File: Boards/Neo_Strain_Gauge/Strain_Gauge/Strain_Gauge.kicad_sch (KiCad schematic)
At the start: 70 parts, among them J1 Screw_Terminal_01x03, J2 Screw_Terminal_01x03, J3 Screw_Terminal_01x03, J4 Screw_Terminal_01x03, J5 Conn_01x02, J6 USB_B_Micro, J7 Conn_02x10_Counter_Clockwise, J8 Conn_02x12_Counter_Clockwise, U1 W25Q128JVS, U2 NCP1117-3.3_SOT223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

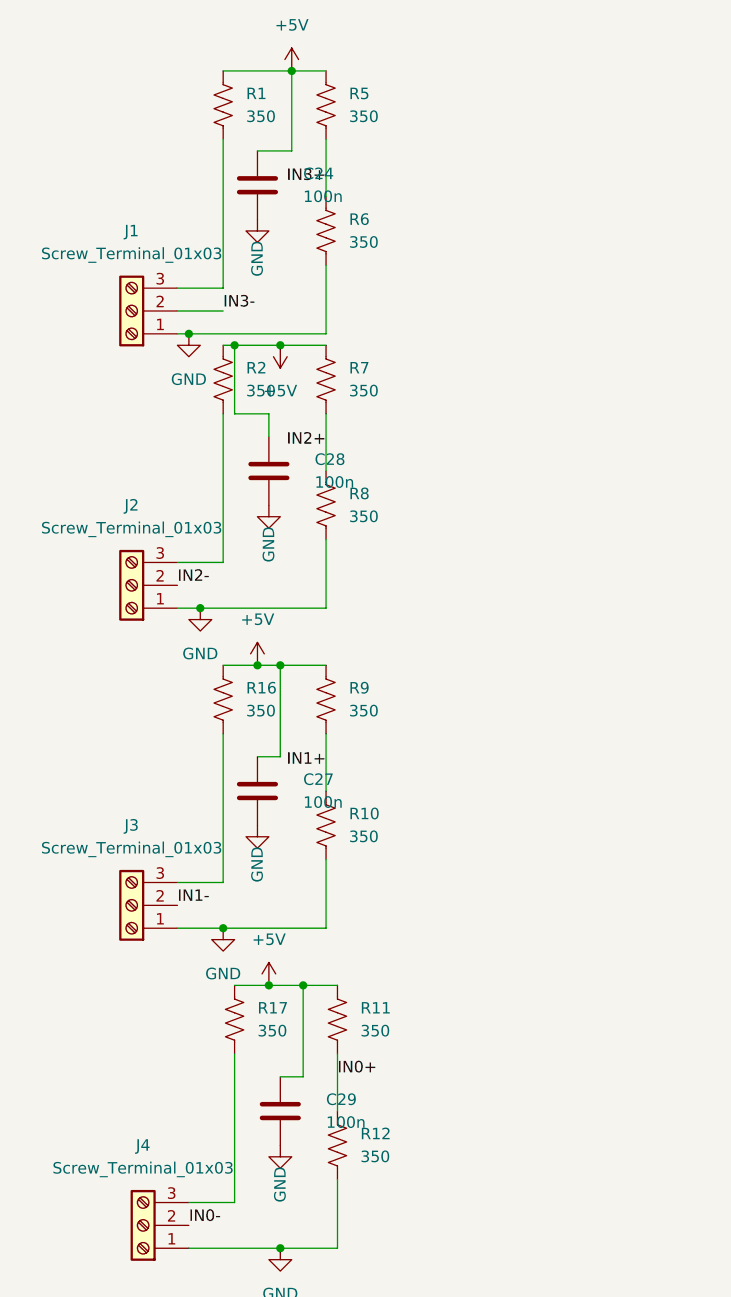
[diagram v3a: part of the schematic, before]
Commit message: Better BOM and more accurate to final design schematic, little will change from this.
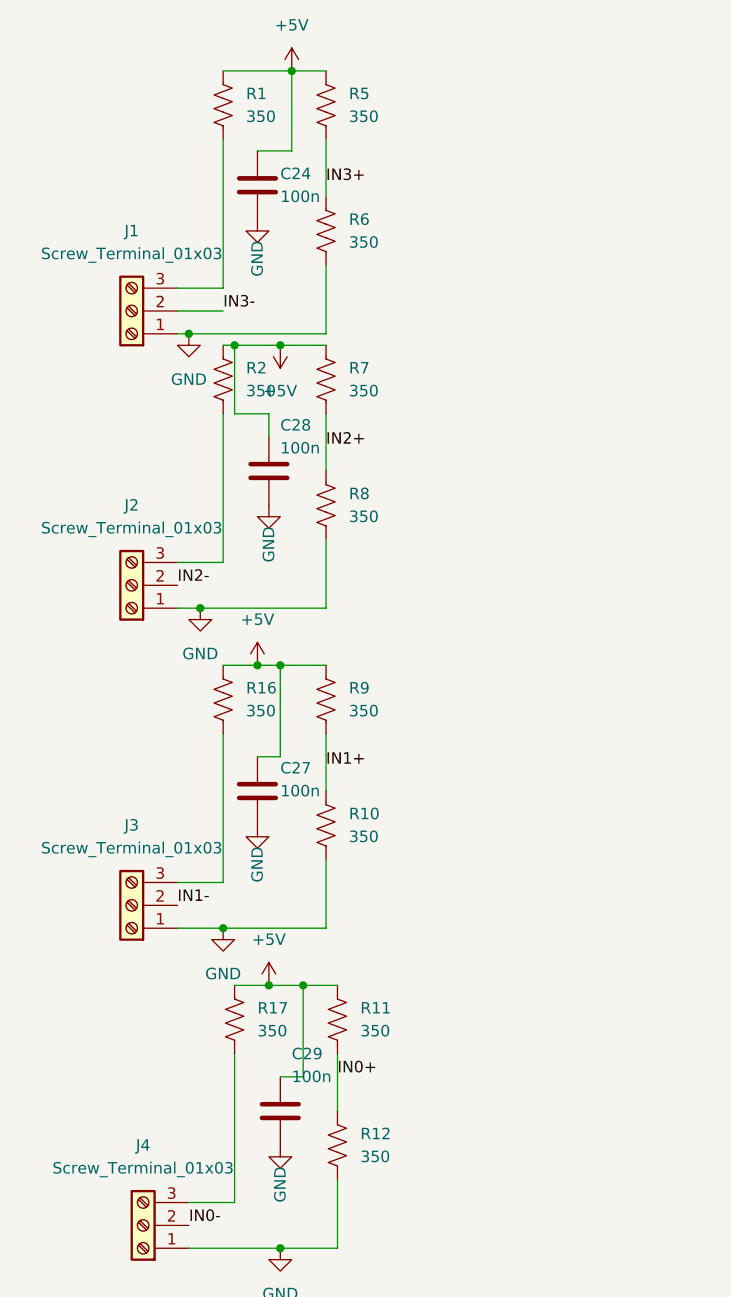
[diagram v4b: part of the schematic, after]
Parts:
- J1, J2, J3, J4: footprint TerminalBlock:TerminalBlock_Altech_AK300-3_P5.00mm -> TerminalBlock_Phoenix:TerminalBlock_Phoenix_PT-1,5-3-3.5-H_1x03_P3.50mm_Horizontal; Purchase Link (none) -> https://www.digikey.com/en/products/detail/phoenix-contact/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
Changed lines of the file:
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@@
     (effects (font (size 1.27 1.27)) (justify right bottom))
   )
-  (label "IN1+" (at -217.17 331.47 180)
-    (effects (font (size 1.27 1.27)) (justify right bottom))
+  (label "IN1+" (at -217.17 331.47 0)
+    (effects (font (size 1.27 1.27)) (justify left bottom))
   )
   (label "GPIO28_ADC2" (at 238.76 417.83 180)
@@
     (effects (font (size 1.27 1.27)) (justify right bottom))
   )
-  (label "IN3+" (at -217.17 266.609 180)
-    (effects (font (size 1.27 1.27)) (justify right bottom))
+  (label "IN3+" (at -217.17 266.609 0)
+    (effects (font (size 1.27 1.27)) (justify left bottom))
   )
   (label "USB_D+" (at 242.57 267.97 180)
@@
     (effects (font (size 1.27 1.27)) (justify right bottom))
   )
-  (label "IN2+" (at -217.17 295.91 180)
-    (effects (font (size 1.27 1.27)) (justify right bottom))
+  (label "IN2+" (at -217.17 295.91 0)
+    (effects (font (size 1.27 1.27)) (justify left bottom))
   )
   (label "GPIO7" (at 406.4 332.74 180)
@@
   )
   (symbol (lib_id "Device:C") (at -223.52 298.45 180) (unit 1)
-    (in_bom yes) (on_board yes) (fields_autoplaced)
-    (property "Reference" "C28" (id 0) (at -218.44 297.1799 0)
+    (in_bom yes) (on_board yes)
+    (property "Reference" "C28" (id 0) (at -222.25 293.37 0)
       (effects (font (size 1.27 1.27)) (justify right))
     )
-    (property "Value" "100n" (id 1) (at -218.44 299.7199 0)
+    (property "Value" "100n" (id 1) (at -222.25 295.91 0)
       (effects (font (size 1.27 1.27)) (justify right))
     )
@@
   )
   (symbol (lib_id "Device:C") (at -224.79 266.7 180) (unit 1)
-    (in_bom yes) (on_board yes) (fields_autoplaced)
-    (property "Reference" "C24" (id 0) (at -219.71 265.4299 0)
+    (in_bom yes) (on_board yes)
+    (property "Reference" "C24" (id 0) (at -222.25 265.43 0)
       (effects (font (size 1.27 1.27)) (justify right))
     )
-    (property "Value" "100n" (id 1) (at -219.71 267.9699 0)
+    (property "Value" "100n" (id 1) (at -222.25 267.97 0)
       (effects (font (size 1.27 1.27)) (justify right))
     )
@@
     (property "Reference" "J3" (id 0) (at -238.76 337.82 0))
     (property "Value" "Screw_Terminal_01x03" (id 1) (at -238.76 340.36 0))
-    (property "Footprint" "TerminalBlock:TerminalBlock_Altech_AK300-3_P5.00mm" (id 2) (at -238.76 346.71 0)
+    (property "Footprint" "TerminalBlock_Phoenix:TerminalBlock_Phoenix_PT-1,5-3-3.5-H_1x03_P3.50mm_Horizontal" (id 2) (at -238.76 346.71 0)
       (effects (font (size 1.27 1.27)) hide)
     )
@@
       (effects (font (size 1.27 1.27)) hide)
     )
+    (property "Purchase Link" "https://www.digikey.com/en/products/detail/phoenix-contact/1751251/2511152" (id 4) (at -238.76 346.71 0)
+      (effects (font (size 1.27 1.27)) hide)
+    )
     (pin "1")
     (pin "2")
@@
     (property "Reference" "J1" (id 0) (at -238.76 271.78 0))
     (property "Value" "Screw_Terminal_01x03" (id 1) (at -238.76 274.32 0))
-    (property "Footprint" "TerminalBlock:TerminalBlock_Altech_AK300-3_P5.00mm" (id 2) (at -238.76 280.67 0)
+    (property "Footprint" "TerminalBlock_Phoenix:TerminalBlock_Phoenix_PT-1,5-3-3.5-H_1x03_P3.50mm_Horizontal" (id 2) (at -238.76 280.67 0)
       (effects (font (size 1.27 1.27)) hide)
     )
@@
       (effects (font (size 1.27 1.27)) hide)
     )
+    (property "Purchase Link" "https://www.digikey.com/en/products/detail/phoenix-contact/1751251/2511152" (id 4) (at -238.76 280.67 0)
+      (effects (font (size 1.27 1.27)) hide)
+    )
     (pin "1")
     (pin "2")
@@
   )
   (symbol (lib_id "Device:C") (at -222.25 369.57 180) (unit 1)
-    (in_bom yes) (on_board yes) (fields_autoplaced)
-    (property "Reference" "C29" (id 0) (at -217.17 368.2999 0)
+    (in_bom yes) (on_board yes)
+    (property "Reference" "C29" (id 0) (at -220.98 363.22 0)
       (effects (font (size 1.27 1.27)) (justify right))
     )
-    (property "Value" "100n" (id 1) (at -217.17 370.8399 0)
+    (property "Value" "100n" (id 1) (at -220.98 365.76 0)
       (effects (font (size 1.27 1.27)) (justify right))
     )
@@
     (property "Reference" "J2" (id 0) (at -238.76 302.26 0))
     (property "Value" "Screw_Terminal_01x03" (id 1) (at -238.76 304.8 0))
-    (property "Footprint" "TerminalBlock:TerminalBlock_Altech_AK300-3_P5.00mm" (id 2) (at -238.76 311.15 0)
+    (property "Footprint" "TerminalBlock_Phoenix:TerminalBlock_Phoenix_PT-1,5-3-3.5-H_1x03_P3.50mm_Horizontal" (id 2) (at -238.76 311.15 0)
       (effects (font (size 1.27 1.27)) hide)
     )
@@
       (effects (font (size 1.27 1.27)) hide)
     )
+    (property "Purchase Link" "https://www.digikey.com/en/products/detail/phoenix-contact/1751251/2511152" (id 4) (at -238.76 311.15 0)
+      (effects (font (size 1.27 1.27)) hide)
+    )
     (pin "1")
     (pin "2")
@@
   )
   (symbol (lib_id "Device:C") (at -224.79 334.01 180) (unit 1)
-    (in_bom yes) (on_board yes) (fields_autoplaced)
-    (property "Reference" "C27" (id 0) (at -219.71 332.7399 0)
+    (in_bom yes) (on_board yes)
+    (property "Reference" "C27" (id 0) (at -222.25 331.47 0)
       (effects (font (size 1.27 1.27)) (justify right))
     )
-    (property "Value" "100n" (id 1) (at -219.71 335.2799 0)
+    (property "Value" "100n" (id 1) (at -222.25 334.01 0)
       (effects (font (size 1.27 1.27)) (justify right))
     )
@@
     (property "Reference" "J4" (id 0) (at -237.49 373.38 0))
     (property "Value" "Screw_Terminal_01x03" (id 1) (at -237.49 375.92 0))
-    (property "Footprint" "TerminalBlock:TerminalBlock_Altech_AK300-3_P5.00mm" (id 2) (at -237.49 382.27 0)
+    (property "Footprint" "TerminalBlock_Phoenix:TerminalBlock_Phoenix_PT-1,5-3-3.5-H_1x03_P3.50mm_Horizontal" (id 2) (at -237.49 382.27 0)
       (effects (font (size 1.27 1.27)) hide)
     )
@@
       (effects (font (size 1.27 1.27)) hide)
     )
+    (property "Purchase Link" "https://www.digikey.com/en/products/detail/phoenix-contact/1751251/2511152" (id 4) (at -237.49 382.27 0)
+      (effects (font (size 1.27 1.27)) hide)
+    )
     (pin "1")
     (pin "2")
@@
     )
     (path "/812efec1-5e5a-41fb-9690-ca97371b7144"
-      (reference "J1") (unit 1) (value "Screw_Terminal_01x03") (footprint "TerminalBlock:TerminalBlock_Altech_AK300-3_P5.00mm")
+      (reference "J1") (unit 1) (value "Screw_Terminal_01x03") (footprint "TerminalBlock_Phoenix:TerminalBlock_Phoenix_PT-1,5-3-3.5-H_1x03_P3.50mm_Horizontal")
     )
     (path "/d8b70fd1-240b-4977-9a3d-4da242adf4b9"
-      (reference "J2") (unit 1) (value "Screw_Terminal_01x03") (footprint "TerminalBlock:TerminalBlock_Altech_AK300-3_P5.00mm")
+      (reference "J2") (unit 1) (value "Screw_Terminal_01x03") (footprint "TerminalBlock_Phoenix:TerminalBlock_Phoenix_PT-1,5-3-3.5-H_1x03_P3.50mm_Horizontal")
     )
     (path "/7775c373-c9d9-4cfb-9d30-eae62f31f8c5"
-      (reference "J3") (unit 1) (value "Screw_Terminal_01x03") (footprint "TerminalBlock:TerminalBlock_Altech_AK300-3_P5.00mm")
+      (reference "J3") (unit 1) (value "Screw_Terminal_01x03") (footprint "TerminalBlock_Phoenix:TerminalBlock_Phoenix_PT-1,5-3-3.5-H_1x03_P3.50mm_Horizontal")
     )
     (path "/fdbaacd7-bf3c-4719-88f6-df0fd5325f84"
-      (reference "J4") (unit 1) (value "Screw_Terminal_01x03") (footprint "TerminalBlock:TerminalBlock_Altech_AK300-3_P5.00mm")
+      (reference "J4") (unit 1) (value "Screw_Terminal_01x03") (footprint "TerminalBlock_Phoenix:TerminalBlock_Phoenix_PT-1,5-3-3.5-H_1x03_P3.50mm_Horizontal")
     )
     (path "/1c1af9d0-8243-4e25-b4e9-4621e89da521"

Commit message: Switch to standard pin header widths.
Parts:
- J5: Purchase Link (none) -> https://www.digikey.com/en/products/detail/gct/BC020-02-A-0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
- J7: Purchase Link https://www.digikey.com/en/products/detail/adam-tech/RS2-20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 -> https://www.digikey.com/en/products/detail/samtec-inc/SSQ-1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
- J8: Purchase Link (none) -> https://www.digikey.com/en/products/detail/samtec-inc/SSQ-1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
- JP2, JP3, JP4, JP5: footprint Connector_PinHeader_2.00mm:PinHeader_1x03_P2.00mm_Vertical -> Connector_PinHeader_2.54mm:PinHeader_1x03_P2.54mm_Vertical; Purchase Link (none) -> https://www.digikey.com/en/products/detail/w%C3%BCrth-elekt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
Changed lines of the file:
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@@
       (effects (font (size 1.27 1.27)) (justify left))
     )
-    (property "Footprint" "Connector_PinHeader_2.00mm:PinHeader_1x03_P2.00mm_Vertical" (id 2) (at 396.24 430.53 0)
+    (property "Footprint" "Connector_PinHeader_2.54mm:PinHeader_1x03_P2.54mm_Vertical" (id 2) (at 396.24 430.53 0)
       (effects (font (size 1.27 1.27)) hide)
     )
     (property "Datasheet" "~" (id 3) (at 396.24 430.53 0)
+      (effects (font (size 1.27 1.27)) hide)
+    )
+    (property "Purchase Link" "https://www.digikey.com/en/products/detail/w%C3%BCrth-elektronik/61300211121/4846823" (id 4) (at 396.24 430.53 0)
       (effects (font (size 1.27 1.27)) hide)
     )
@@
     )
     (property "Datasheet" "~" (id 3) (at 187.96 328.93 0)
+      (effects (font (size 1.27 1.27)) hide)
+    )
+    (property "Purchase Link" "https://www.digikey.com/en/products/detail/gct/BC020-02-A-0200-0300-L-G/12549946" (id 4) (at 187.96 328.93 0)
       (effects (font (size 1.27 1.27)) hide)
     )
@@
       (effects (font (size 1.27 1.27)) (justify left))
     )
-    (property "Footprint" "Connector_PinHeader_2.00mm:PinHeader_1x03_P2.00mm_Vertical" (id 2) (at 462.28 429.26 0)
+    (property "Footprint" "Connector_PinHeader_2.54mm:PinHeader_1x03_P2.54mm_Vertical" (id 2) (at 462.28 429.26 0)
       (effects (font (size 1.27 1.27)) hide)
     )
     (property "Datasheet" "~" (id 3) (at 462.28 429.26 0)
+      (effects (font (size 1.27 1.27)) hide)
+    )
+    (property "Purchase Link" "https://www.digikey.com/en/products/detail/w%C3%BCrth-elektronik/61300211121/4846823" (id 4) (at 462.28 429.26 0)
       (effects (font (size 1.27 1.27)) hide)
     )
@@
     )
     (property "Datasheet" "~" (id 3) (at 144.78 356.87 0)
+      (effects (font (size 1.27 1.27)) hide)
+    )
+    (property "Purchase Link" "https://www.digikey.com/en/products/detail/samtec-inc/SSQ-106-03-G-D/1111457?s=N4IgTCBcDaIMoEECyBGFBOAbAWgAw4DkAREAXQF8g" (id 4) (at 144.78 356.87 0)
       (effects (font (size 1.27 1.27)) hide)
     )
@@
       (effects (font (size 1.27 1.27)) (justify left))
     )
-    (property "Footprint" "Connector_PinHeader_2.00mm:PinHeader_1x03_P2.00mm_Vertical" (id 2) (at 429.26 429.26 0)
+    (property "Footprint" "Connector_PinHeader_2.54mm:PinHeader_1x03_P2.54mm_Vertical" (id 2) (at 429.26 429.26 0)
       (effects (font (size 1.27 1.27)) hide)
     )
     (property "Datasheet" "~" (id 3) (at 429.26 429.26 0)
+      (effects (font (size 1.27 1.27)) hide)
+    )
+    (property "Purchase Link" "https://www.digikey.com/en/products/detail/w%C3%BCrth-elektronik/61300211121/4846823" (id 4) (at 429.26 429.26 0)
       (effects (font (size 1.27 1.27)) hide)
     )
@@
       (effects (font (size 1.27 1.27)) hide)
     )
-    (property "Purchase Link" "https://www.digikey.com/en/products/detail/adam-tech/RS2-20-G/9832051" (id 4) (at 93.98 359.41 0)
+    (property "Purchase Link" "https://www.digikey.com/en/products/detail/samtec-inc/SSQ-105-03-G-D/1111458" (id 4) (at 93.98 359.41 0)
       (effects (font (size 1.27 1.27)) hide)
     )
@@
       (effects (font (size 1.27 1.27)) (justify left))
     )
-    (property "Footprint" "Connector_PinHeader_2.00mm:PinHeader_1x03_P2.00mm_Vertical" (id 2) (at 496.57 429.26 0)
+    (property "Footprint" "Connector_PinHeader_2.54mm:PinHeader_1x03_P2.54mm_Vertical" (id 2) (at 496.57 429.26 0)
       (effects (font (size 1.27 1.27)) hide)
     )
     (property "Datasheet" "~" (id 3) (at 496.57 429.26 0)
+      (effects (font (size 1.27 1.27)) hide)
+    )
+    (property "Purchase Link" "https://www.digikey.com/en/products/detail/w%C3%BCrth-elektronik/61300211121/4846823" (id 4) (at 496.57 429.26 0)
       (effects (font (size 1.27 1.27)) hide)
     )
@@
     )
     (path "/c48eefdb-f27a-44af-bdf1-88a535a72a7e"
-      (reference "JP2") (unit 1) (value "Jumper_3_Open") (footprint "Connector_PinHeader_2.00mm:PinHeader_1x03_P2.00mm_Vertical")
+      (reference "JP2") (unit 1) (value "Jumper_3_Open") (footprint "Connector_PinHeader_2.54mm:PinHeader_1x03_P2.54mm_Vertical")
     )
     (path "/278653bb-d9e2-4d1f-82ef-015d0063ca19"
-      (reference "JP3") (unit 1) (value "Jumper_3_Open") (footprint "Connector_PinHeader_2.00mm:PinHeader_1x03_P2.00mm_Vertical")
+      (reference "JP3") (unit 1) (value "Jumper_3_Open") (footprint "Connector_PinHeader_2.54mm:PinHeader_1x03_P2.54mm_Vertical")
     )
     (path "/b5fe66cd-27ee-4c86-a86d-305078b4362d"
-      (reference "JP4") (unit 1) (value "Jumper_3_Open") (footprint "Connector_PinHeader_2.00mm:PinHeader_1x03_P2.00mm_Vertical")
+      (reference "JP4") (unit 1) (value "Jumper_3_Open") (footprint "Connector_PinHeader_2.54mm:PinHeader_1x03_P2.54mm_Vertical")
     )
     (path "/0cf9660d-9563-496b-b969-833d7c6611dd"
-      (reference "JP5") (unit 1) (value "Jumper_3_Open") (footprint "Connector_PinHeader_2.00mm:PinHeader_1x03_P2.00mm_Vertical")
+      (reference "JP5") (unit 1) (value "Jumper_3_Open") (footprint "Connector_PinHeader_2.54mm:PinHeader_1x03_P2.54mm_Vertical")
     )
     (path "/d89e76b3-4fff-4982-8d9a-95afa00617eb"

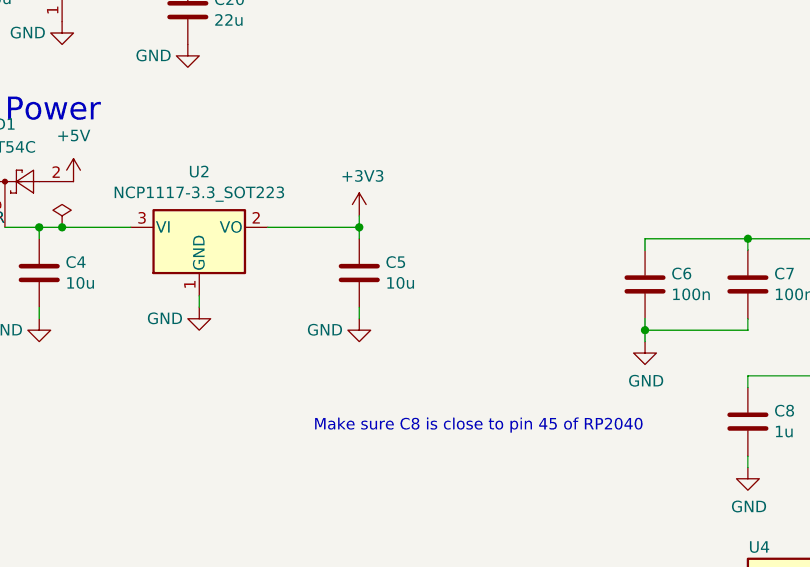
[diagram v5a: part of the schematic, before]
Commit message: Replacement part due to parts shortage.
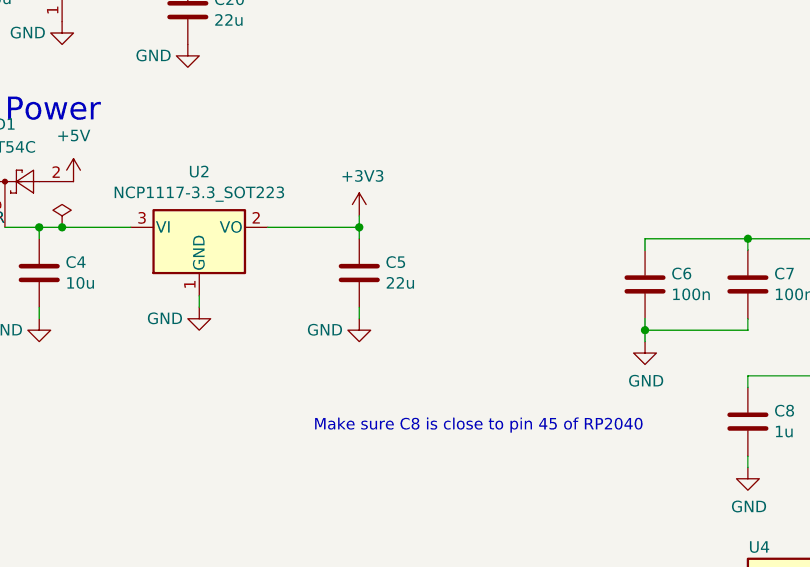
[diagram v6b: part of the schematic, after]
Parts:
- C5: value 10u -> 22u; Purchase Link https://www.digikey.com/en/products/detail/murata-electroni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 -> https://www.digikey.com/en/products/detail/samsung-electro-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
- U2: Purchase Link https://www.digikey.com/en/products/detail/onsemi/NCP1117LP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 -> https://www.digikey.com/en/products/detail/dcomponents/LDI1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
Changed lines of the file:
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@@
     (pin "1")
+  )
+  (symbol (lib_id "Device:C") (at 287.02 267.97 0) (unit 1)
+    (in_bom yes) (on_board yes)
+    (property "Reference" "C5" (id 0) (at 289.941 266.8016 0)
+      (effects (font (size 1.27 1.27)) (justify left))
+    )
+    (property "Value" "22u" (id 1) (at 289.941 269.113 0)
+      (effects (font (size 1.27 1.27)) (justify left))
+    )
+    (property "Footprint" "Capacitor_SMD:C_0603_1608Metric" (id 2) (at 287.9852 271.78 0)
+      (effects (font (size 1.27 1.27)) hide)
+    )
+    (property "Datasheet" "~" (id 3) (at 287.02 267.97 0)
+      (effects (font (size 1.27 1.27)) hide)
+    )
+    (property "Purchase Link" "https://www.digikey.com/en/products/detail/samsung-electro-mechanics/CL10A226MP8NUNE/3886932" (id 4) (at 287.02 267.97 0)
+      (effects (font (size 1.27 1.27)) hide)
+    )
+    (pin "1")
+    (pin "2")
   )
   (symbol (lib_id "Logic_LevelTranslator:TXB0104RGY") (at 248.92 415.29 0) (unit 1)
@@
     )
     (pin "1")
-  )
-  (symbol (lib_id "Device:C") (at 287.02 267.97 0) (unit 1)
-    (in_bom yes) (on_board yes)
-    (property "Reference" "C5" (id 0) (at 289.941 266.8016 0)
-      (effects (font (size 1.27 1.27)) (justify left))
-    )
-    (property "Value" "10u" (id 1) (at 289.941 269.113 0)
-      (effects (font (size 1.27 1.27)) (justify left))
-    )
-    (property "Footprint" "Capacitor_SMD:C_0603_1608Metric" (id 2) (at 287.9852 271.78 0)
-      (effects (font (size 1.27 1.27)) hide)
-    )
-    (property "Datasheet" "~" (id 3) (at 287.02 267.97 0)
-      (effects (font (size 1.27 1.27)) hide)
-    )
-    (property "Purchase Link" "https://www.digikey.com/en/products/detail/murata-electronics/GRT188C81A106ME13D/5416705" (id 4) (at 287.02 267.97 0)
-      (effects (font (size 1.27 1.27)) hide)
-    )
-    (pin "1")
-    (pin "2")
   )
   (symbol (lib_id "Device:R_US") (at -215.9 373.38 0) (unit 1)
@@
       (effects (font (size 1.27 1.27)) hide)
     )
-    (property "Purchase Link" "https://www.digikey.com/en/products/detail/onsemi/NCP1117LPST33T3G/2194024" (id 4) (at 269.24 262.89 0)
+    (property "Purchase Link" "https://www.digikey.com/en/products/detail/dcomponents/LDI1117-3-3H/15850431" (id 4) (at 269.24 262.89 0)
       (effects (font (size 1.27 1.27)) hide)
     )
@@
       (reference "C4") (unit 1) (value "10u") (footprint "Capacitor_SMD:C_0603_1608Metric")
     )
-    (path "/88bc9d99-afa2-40e7-b578-1b4cda291bf5"
-      (reference "C5") (unit 1) (value "10u") (footprint "Capacitor_SMD:C_0603_1608Metric")
+    (path "/7d83ab8b-70b4-47b3-935e-77c9099fb251"
+      (reference "C5") (unit 1) (value "22u") (footprint "Capacitor_SMD:C_0603_1608Metric")
     )
     (path "/529d4787-c2ad-4cac-b965-6023d119175e"

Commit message: Ensure strain gauge board uses cheaper components
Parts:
- R1, R10, R11, R12, R16, R17, R5, R6, R7, R8, R9: footprint Resistor_SMD:R_0805_2012Metric -> Resistor_SMD:R_1206_3216Metric
- R2: footprint Resistor_SMD:R_0805_2012Metric -> Resistor_SMD:R_1210_3225Metric
